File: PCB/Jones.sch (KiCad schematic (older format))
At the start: 250 parts, among them J1 USB_C_Receptacle_USB2.0, J2 Conn_01x03, J3 Conn_01x02, J5 Conn_02x03_Odd_Even, U1 ATmega32U4-MU, U2 24LC64, Y1 16MHz

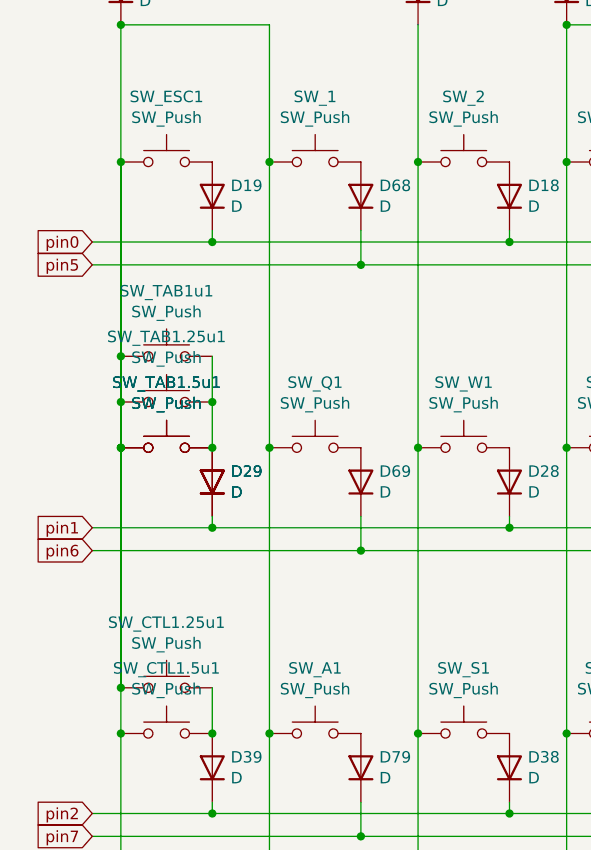
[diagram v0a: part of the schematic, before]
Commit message: issue レイアウト：40sキット対応 #29
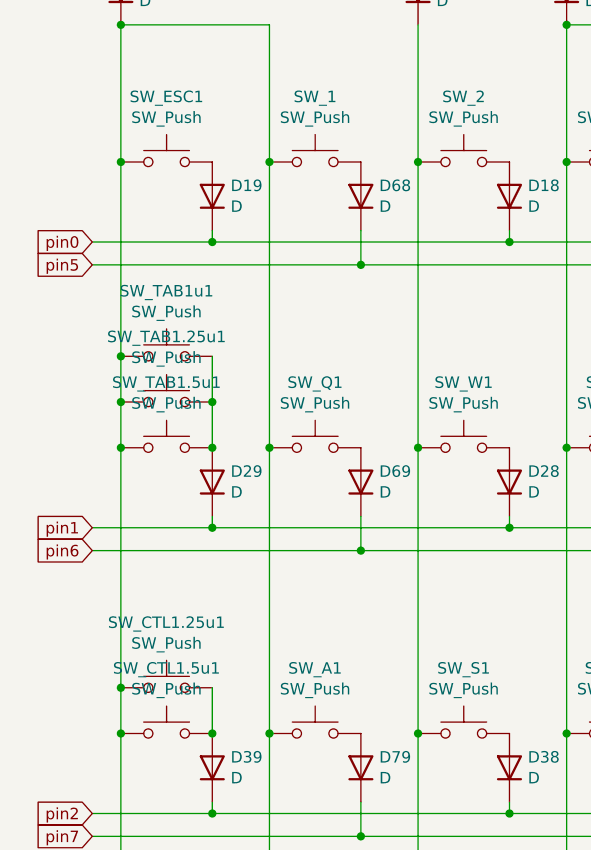
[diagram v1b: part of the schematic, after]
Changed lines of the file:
@@
 $EndComp
 $Comp
-L Device:D D29
-U 1 1 5F65B339
-P 1325 3475
-F 0 "D29" V 1371 3395 50  0000 R CNN
-F 1 "D" V 1280 3395 50  0000 R CNN
-F 2 "Diode_SMD:D_SOD-123" H 1325 3475 50  0001 C CNN
-F 3 "~" H 1325 3475 50  0001 C CNN
-F 4 "C81598" H 1325 3475 50  0001 C CNN "LCSC"
-	1    1325 3475
-	0    -1   -1   0
-$EndComp
-$Comp
 L Switch:SW_Push SW_Q1
 U 1 1 5F65B33F
@@
 	0    -1   -1   0
 $EndComp
-$Comp
-L Switch:SW_Push SW_TAB1.5u1
-U 1 1 5F65B333
-P 1125 3325
-F 0 "SW_TAB1.5u1" H 1125 3610 50  0000 C CNN
-F 1 "SW_Push" H 1125 3519 50  0000 C CNN
-F 2 "MX_Alps_Hybrid:MXOnly-1.5U-Hotswap-guide" H 1125 3525 50  0001 C CNN
-F 3 "~" H 1125 3525 50  0001 C CNN
-	1    1125 3325
-	1    0    0    -1
-$EndComp
 Wire Wire Line
 	925  1475 1575 1475
@@
 Wire Wire Line
 	800  2425 1325 2425
-Connection ~ 925  3325
 Wire Wire Line
 	800  3675 1325 3675
-Wire Wire Line
-	925  3325 925  4375
 Connection ~ 925  4375
 Connection ~ 925  4575
@@
 Text Notes 14450 3725 0    50   ~ 0
 Audio\nC4,5,6\nB5,6,7
-Wire Wire Line
-	925  2075 925  3325
 Connection ~ 925  2075
 $Comp

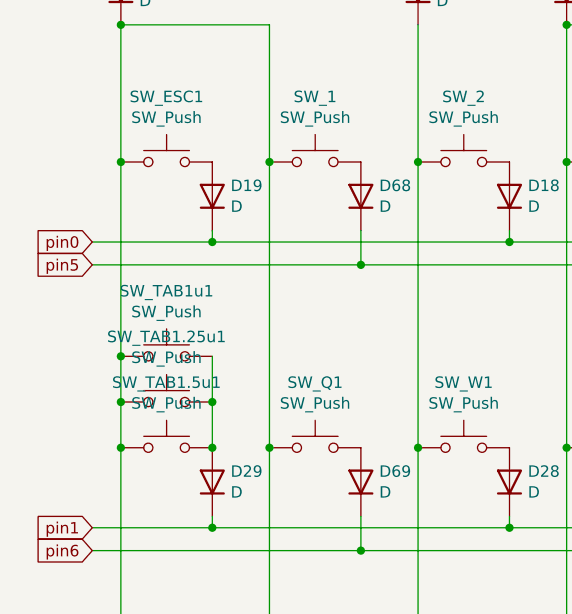
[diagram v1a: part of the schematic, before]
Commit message: Revert "Merge pull request #36 from jpskenn/dev_1.1_Add_40s_layout_#29"
This reverts commit ac7df7e95556fcbf06f35e39de5424a1bd39dfc1, reversing
changes made to 127994836709470240343b38cf9ba11c4b8eb1ff.
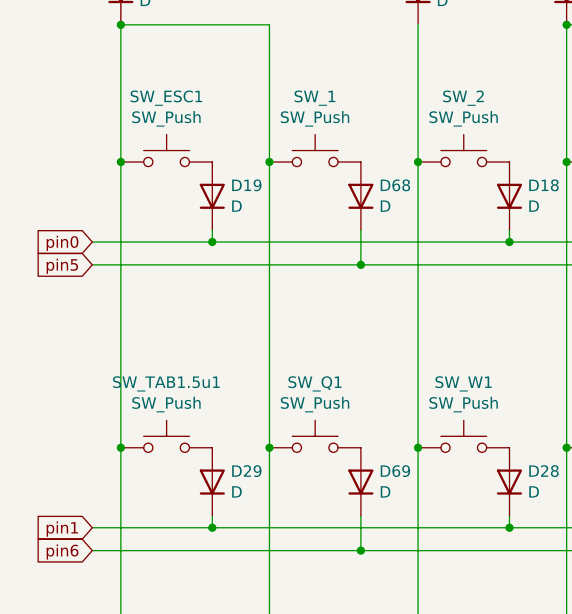
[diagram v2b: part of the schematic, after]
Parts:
- removed SW_TAB1.25u1: SW_Push, MX_Alps_Hybrid:MXOnly-1.25U-Hotswap-guide-Rotate, symbol Switch:SW_Push
- removed SW_TAB1u1: SW_Push, MX_Alps_Hybrid:MXOnly-1U-Hotswap-guide-4pin, symbol Switch:SW_Push
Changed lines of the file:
@@
 $EndComp
 $Comp
+L Device:D D29
+U 1 1 5F65B339
+P 1325 3475
+F 0 "D29" V 1371 3395 50  0000 R CNN
+F 1 "D" V 1280 3395 50  0000 R CNN
+F 2 "Diode_SMD:D_SOD-123" H 1325 3475 50  0001 C CNN
+F 3 "~" H 1325 3475 50  0001 C CNN
+F 4 "C81598" H 1325 3475 50  0001 C CNN "LCSC"
+	1    1325 3475
+	0    -1   -1   0
+$EndComp
+$Comp
 L Switch:SW_Push SW_Q1
 U 1 1 5F65B33F
@@
 	0    -1   -1   0
 $EndComp
+$Comp
+L Switch:SW_Push SW_TAB1.5u1
+U 1 1 5F65B333
+P 1125 3325
+F 0 "SW_TAB1.5u1" H 1125 3610 50  0000 C CNN
+F 1 "SW_Push" H 1125 3519 50  0000 C CNN
+F 2 "MX_Alps_Hybrid:MXOnly-1.5U-Hotswap-guide" H 1125 3525 50  0001 C CNN
+F 3 "~" H 1125 3525 50  0001 C CNN
+	1    1125 3325
+	1    0    0    -1
+$EndComp
 Wire Wire Line
 	925  1475 1575 1475
@@
 Wire Wire Line
 	800  2425 1325 2425
+Connection ~ 925  3325
 Wire Wire Line
 	800  3675 1325 3675
+Wire Wire Line
+	925  3325 925  4375
 Connection ~ 925  4375
 Connection ~ 925  4575
@@
 Text Notes 14450 3725 0    50   ~ 0
 Audio\nC4,5,6\nB5,6,7
+Wire Wire Line
+	925  2075 925  3325
 Connection ~ 925  2075
 $Comp
@@
 Wire Wire Line
 	14725 1575 14825 1575
-Wire Wire Line
-	925  2075 925  2925
-Wire Wire Line
-	925  3325 925  4375
-Connection ~ 925  3325
-$Comp
-L Switch:SW_Push SW_TAB1.5u1
-U 1 1 5F65B333
-P 1125 3325
-F 0 "SW_TAB1.5u1" H 1125 3610 50  0000 C CNN
-F 1 "SW_Push" H 1125 3519 50  0000 C CNN
-F 2 "MX_Alps_Hybrid:MXOnly-1.5U-Hotswap-guide" H 1125 3525 50  0001 C CNN
-F 3 "~" H 1125 3525 50  0001 C CNN
-	1    1125 3325
-	1    0    0    -1
-$EndComp
-$Comp
-L Device:D D29
-U 1 1 5F65B339
-P 1325 3475
-F 0 "D29" V 1371 3395 50  0000 R CNN
-F 1 "D" V 1280 3395 50  0000 R CNN
-F 2 "Diode_SMD:D_SOD-123" H 1325 3475 50  0001 C CNN
-F 3 "~" H 1325 3475 50  0001 C CNN
-F 4 "C81598" H 1325 3475 50  0001 C CNN "LCSC"
-	1    1325 3475
-	0    -1   -1   0
-$EndComp
-$Comp
-L Switch:SW_Push SW_TAB1.25u1
-U 1 1 615879B4
-P 1125 3125
-F 0 "SW_TAB1.25u1" H 1125 3410 50  0000 C CNN
-F 1 "SW_Push" H 1125 3319 50  0000 C CNN
-F 2 "MX_Alps_Hybrid:MXOnly-1.25U-Hotswap-guide-Rotate" H 1125 3325 50  0001 C CNN
-F 3 "~" H 1125 3325 50  0001 C CNN
-	1    1125 3125
-	1    0    0    -1
-$EndComp
-$Comp
-L Switch:SW_Push SW_TAB1u1
-U 1 1 615B818E
-P 1125 2925
-F 0 "SW_TAB1u1" H 1125 3210 50  0000 C CNN
-F 1 "SW_Push" H 1125 3119 50  0000 C CNN
-F 2 "MX_Alps_Hybrid:MXOnly-1U-Hotswap-guide-4pin" H 1125 3125 50  0001 C CNN
-F 3 "~" H 1125 3125 50  0001 C CNN
-	1    1125 2925
-	1    0    0    -1
-$EndComp
-Connection ~ 925  2925
-Wire Wire Line
-	925  2925 925  3125
-Connection ~ 925  3125
-Wire Wire Line
-	925  3125 925  3325
-Wire Wire Line
-	1325 2925 1325 3125
-Connection ~ 1325 3325
-Connection ~ 1325 3125
-Wire Wire Line
-	1325 3125 1325 3325
 $EndSCHEMATC

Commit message: 回路図更新。PCBテスト中
回路図、R2のTabに1uと1.25uを追加。
PCB、1uの配置が決まらず、試行錯誤中。
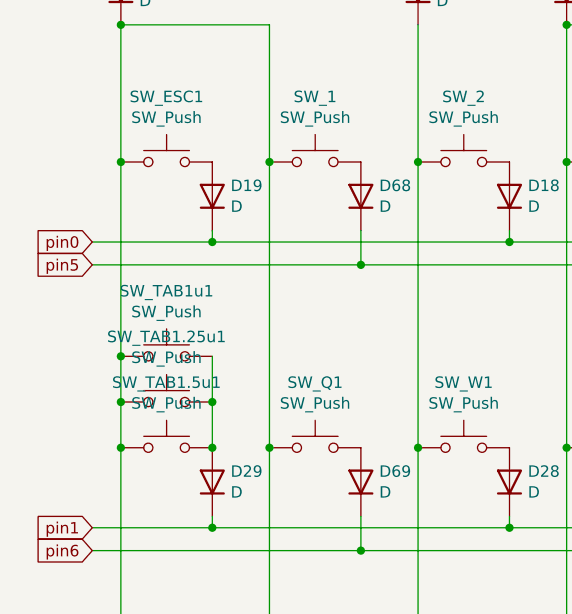
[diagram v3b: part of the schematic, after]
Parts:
- added SW_TAB1.25u1: SW_Push, MX_Alps_Hybrid:MXOnly-1.25U-Hotswap-guide-Rotate, symbol Switch:SW_Push
- added SW_TAB1u1: SW_Push, MX_Alps_Hybrid:MXOnly-1U-Hotswap-guide, symbol Switch:SW_Push
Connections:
- net RE2_1: now also SW_TAB1.25u1.1, SW_TAB1u1.1
- net at D29.2 (A), SW_TAB1.5u1.2: now also SW_TAB1.25u1.2, SW_TAB1u1.2
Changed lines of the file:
@@
 $EndComp
 $Comp
-L Device:D D29
-U 1 1 5F65B339
-P 1325 3475
-F 0 "D29" V 1371 3395 50  0000 R CNN
-F 1 "D" V 1280 3395 50  0000 R CNN
-F 2 "Diode_SMD:D_SOD-123" H 1325 3475 50  0001 C CNN
-F 3 "~" H 1325 3475 50  0001 C CNN
-F 4 "C81598" H 1325 3475 50  0001 C CNN "LCSC"
-	1    1325 3475
-	0    -1   -1   0
-$EndComp
-$Comp
 L Switch:SW_Push SW_Q1
 U 1 1 5F65B33F
@@
 	0    -1   -1   0
 $EndComp
-$Comp
-L Switch:SW_Push SW_TAB1.5u1
-U 1 1 5F65B333
-P 1125 3325
-F 0 "SW_TAB1.5u1" H 1125 3610 50  0000 C CNN
-F 1 "SW_Push" H 1125 3519 50  0000 C CNN
-F 2 "MX_Alps_Hybrid:MXOnly-1.5U-Hotswap-guide" H 1125 3525 50  0001 C CNN
-F 3 "~" H 1125 3525 50  0001 C CNN
-	1    1125 3325
-	1    0    0    -1
-$EndComp
 Wire Wire Line
 	925  1475 1575 1475
@@
 Wire Wire Line
 	800  2425 1325 2425
-Connection ~ 925  3325
 Wire Wire Line
 	800  3675 1325 3675
-Wire Wire Line
-	925  3325 925  4375
 Connection ~ 925  4375
 Connection ~ 925  4575
@@
 Text Notes 14450 3725 0    50   ~ 0
 Audio\nC4,5,6\nB5,6,7
-Wire Wire Line
-	925  2075 925  3325
 Connection ~ 925  2075
 $Comp
@@
 Wire Wire Line
 	14725 1575 14825 1575
+Wire Wire Line
+	925  2075 925  2925
+Wire Wire Line
+	925  3325 925  4375
+Connection ~ 925  3325
+$Comp
+L Switch:SW_Push SW_TAB1.5u1
+U 1 1 5F65B333
+P 1125 3325
+F 0 "SW_TAB1.5u1" H 1125 3610 50  0000 C CNN
+F 1 "SW_Push" H 1125 3519 50  0000 C CNN
+F 2 "MX_Alps_Hybrid:MXOnly-1.5U-Hotswap-guide" H 1125 3525 50  0001 C CNN
+F 3 "~" H 1125 3525 50  0001 C CNN
+	1    1125 3325
+	1    0    0    -1
+$EndComp
+$Comp
+L Device:D D29
+U 1 1 5F65B339
+P 1325 3475
+F 0 "D29" V 1371 3395 50  0000 R CNN
+F 1 "D" V 1280 3395 50  0000 R CNN
+F 2 "Diode_SMD:D_SOD-123" H 1325 3475 50  0001 C CNN
+F 3 "~" H 1325 3475 50  0001 C CNN
+F 4 "C81598" H 1325 3475 50  0001 C CNN "LCSC"
+	1    1325 3475
+	0    -1   -1   0
+$EndComp
+$Comp
+L Switch:SW_Push SW_TAB1.25u1
+U 1 1 615879B4
+P 1125 3125
+F 0 "SW_TAB1.25u1" H 1125 3410 50  0000 C CNN
+F 1 "SW_Push" H 1125 3319 50  0000 C CNN
+F 2 "MX_Alps_Hybrid:MXOnly-1.25U-Hotswap-guide-Rotate" H 1125 3325 50  0001 C CNN
+F 3 "~" H 1125 3325 50  0001 C CNN
+	1    1125 3125
+	1    0    0    -1
+$EndComp
+$Comp
+L Switch:SW_Push SW_TAB1u1
+U 1 1 615B818E
+P 1125 2925
+F 0 "SW_TAB1u1" H 1125 3210 50  0000 C CNN
+F 1 "SW_Push" H 1125 3119 50  0000 C CNN
+F 2 "MX_Alps_Hybrid:MXOnly-1U-Hotswap-guide" H 1125 3125 50  0001 C CNN
+F 3 "~" H 1125 3125 50  0001 C CNN
+	1    1125 2925
+	1    0    0    -1
+$EndComp
+Connection ~ 925  2925
+Wire Wire Line
+	925  2925 925  3125
+Connection ~ 925  3125
+Wire Wire Line
+	925  3125 925  3325
+Wire Wire Line
+	1325 2925 1325 3125
+Connection ~ 1325 3325
+Connection ~ 1325 3125
+Wire Wire Line
+	1325 3125 1325 3325
 $EndSCHEMATC

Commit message: 40s用、R2のTABに、1u、1.25uを追加
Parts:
- SW_TAB1u1: footprint MX_Alps_Hybrid:MXOnly-1U-Hotswap-guide -> MX_Alps_Hybrid:MXOnly-1U-Hotswap-guide-4pin
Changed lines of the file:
@@
 F 0 "SW_TAB1u1" H 1125 3210 50  0000 C CNN
 F 1 "SW_Push" H 1125 3119 50  0000 C CNN
-F 2 "MX_Alps_Hybrid:MXOnly-1U-Hotswap-guide" H 1125 3125 50  0001 C CNN
+F 2 "MX_Alps_Hybrid:MXOnly-1U-Hotswap-guide-4pin" H 1125 3125 50  0001 C CNN
 F 3 "~" H 1125 3125 50  0001 C CNN
 	1    1125 2925

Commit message: Dの方向マークを太くして視認性向上 #4
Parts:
- D0, D1, D11, D12, D13, D14, D15, D16, D17, D18, D19, D2, D21, D22, D23, D24, D25, D26, D27, D28, D29, D3, D30, D31, D32, D33, D34, D35, D36, D37, D38, D39, D4, D40, D41, D42, D43, D44, D45, D46, D47, D48, D49, D5, D50, D51, D52, D53, D56, D57, D59, D6, D61, D62, D63, D64, D65, D67, D68, D69, D7, D71, D73, D74, D75, D78, D79, D8, D83, D84, D85, D87, D89, D9, D91, D92, D93, D94, D95, D96, D97, D98: footprint Diode_SMD:D_SOD-123 -> locallib:D_SOD-123_bold_marking

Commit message: 三角マークを拡大 #5
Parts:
- LED1, LED2, LED3, LED4: footprint locallib:LED_SK6812MINI_PLCC4_3.5x3.5mm_P1.75mm_TriangleMark -> locallib:LED_SK6812MINI_PLCC4_3.5x3.5mm_P1.75mm_TriangleMark_Bold
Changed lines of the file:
@@
 F 0 "LED1" H 3594 8771 50  0000 L CNN
 F 1 "SK6812MINI" H 3594 8680 50  0000 L CNN
-F 2 "locallib:LED_SK6812MINI_PLCC4_3.5x3.5mm_P1.75mm_TriangleMark" H 3300 8425 50  0001 L TNN
+F 2 "locallib:LED_SK6812MINI_PLCC4_3.5x3.5mm_P1.75mm_TriangleMark_Bold" H 3300 8425 50  0001 L TNN
 F 3 "https://cdn-shop.adafruit.com/product-files/2686/SK6812MINI_REV.01-1-2.pdf" H 3350 8350 50  0001 L TNN
 	1    3250 8725
@@
 F 0 "LED2" H 4194 8771 50  0000 L CNN
 F 1 "SK6812MINI" H 4194 8680 50  0000 L CNN
-F 2 "locallib:LED_SK6812MINI_PLCC4_3.5x3.5mm_P1.75mm_TriangleMark" H 3900 8425 50  0001 L TNN
+F 2 "locallib:LED_SK6812MINI_PLCC4_3.5x3.5mm_P1.75mm_TriangleMark_Bold" H 3900 8425 50  0001 L TNN
 F 3 "https://cdn-shop.adafruit.com/product-files/2686/SK6812MINI_REV.01-1-2.pdf" H 3950 8350 50  0001 L TNN
 	1    3850 8725
@@
 F 0 "LED4" H 6019 9371 50  0000 L CNN
 F 1 "SK6812MINI" H 6019 9280 50  0000 L CNN
-F 2 "locallib:LED_SK6812MINI_PLCC4_3.5x3.5mm_P1.75mm_TriangleMark" H 5725 9025 50  0001 L TNN
+F 2 "locallib:LED_SK6812MINI_PLCC4_3.5x3.5mm_P1.75mm_TriangleMark_Bold" H 5725 9025 50  0001 L TNN
 F 3 "https://cdn-shop.adafruit.com/product-files/2686/SK6812MINI_REV.01-1-2.pdf" H 5775 8950 50  0001 L TNN
 	1    5675 9325
@@
 F 0 "LED3" H 5419 9371 50  0000 L CNN
 F 1 "SK6812MINI" H 5419 9280 50  0000 L CNN
-F 2 "locallib:LED_SK6812MINI_PLCC4_3.5x3.5mm_P1.75mm_TriangleMark" H 5125 9025 50  0001 L TNN
+F 2 "locallib:LED_SK6812MINI_PLCC4_3.5x3.5mm_P1.75mm_TriangleMark_Bold" H 5125 9025 50  0001 L TNN
 F 3 "https://cdn-shop.adafruit.com/product-files/2686/SK6812MINI_REV.01-1-2.pdf" H 5175 8950 50  0001 L TNN
 	1    5075 9325

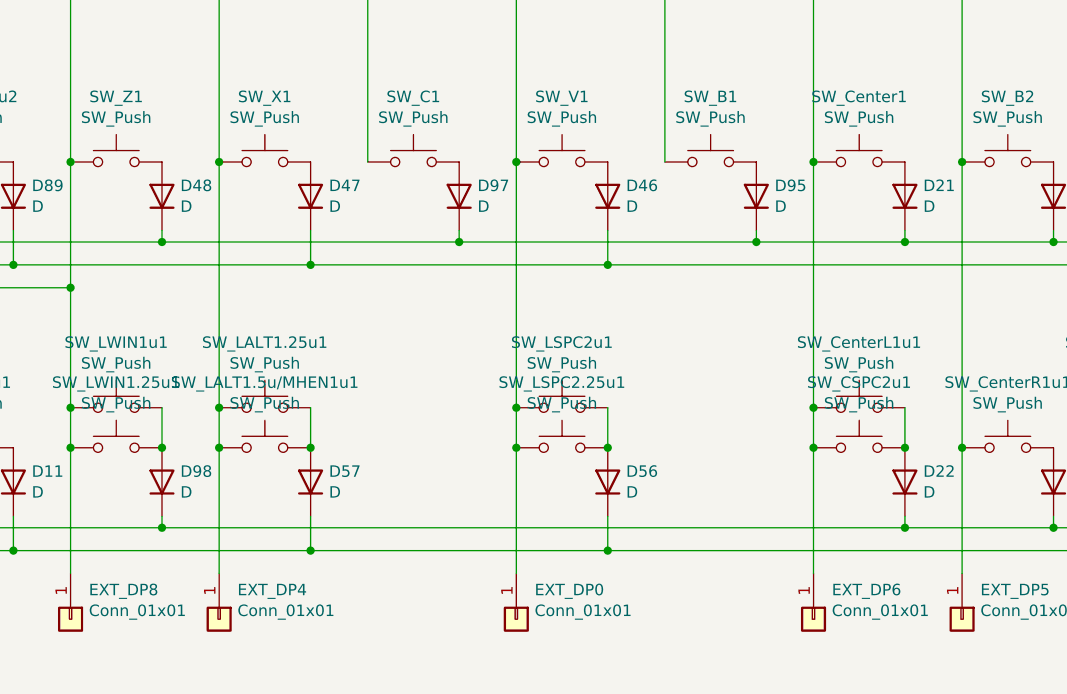
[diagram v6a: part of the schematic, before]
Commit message: WIP：左Modsの回路追加。PCB調整中
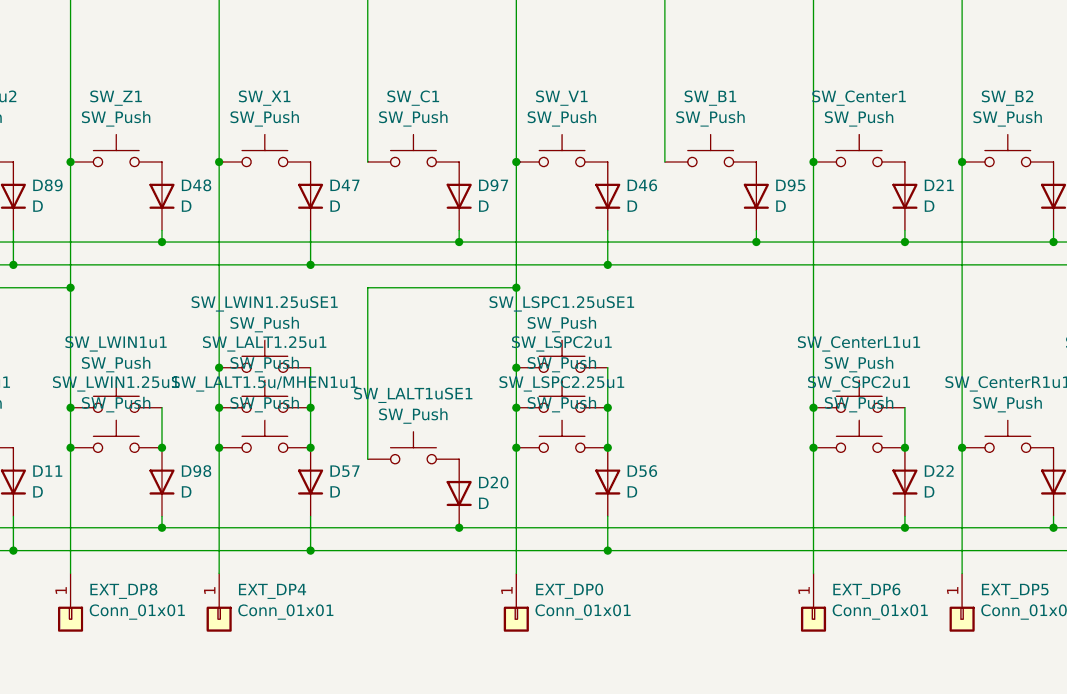
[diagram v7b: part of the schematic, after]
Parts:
- added D20: D, locallib:D_SOD-123_bold_marking, symbol Device:D
- added SW_LALT1uSE1: SW_Push, MX_Alps_Hybrid:MXOnly-1U-NoLED, symbol Switch:SW_Push
- added SW_LSPC1.25uSE1: SW_Push, MX_Alps_Hybrid:MXOnly-1.25U-Hotswap-guide, symbol Switch:SW_Push
- added SW_LWIN1.25uSE1: SW_Push, MX_Alps_Hybrid:MXOnly-1.25U-Hotswap-guide-Rotate, symbol Switch:SW_Push
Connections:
- net pin4: now also D20.1 (K)
- net at D7.1 (K), EXT_DP4.1 (Pin_1), SW_3.1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: now also SW_LWIN1.25uSE1.1
- net at D57.2 (A), SW_LALT1.25u1.2, SW_LALT1.5u/MHEN1u1.2: now also SW_LWIN1.25uSE1.2
- net at D6.1 (K), EXT_DP0.1 (Pin_1), SW_5.1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: now also SW_LALT1uSE1.1, SW_LSPC1.25uSE1.1
- net at D56.2 (A), SW_LSPC2.25u1.2, SW_LSPC2u1.2: now also SW_LSPC1.25uSE1.2
- new net: D20.2 (A), SW_LALT1uSE1.2
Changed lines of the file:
@@
 Connection ~ 3275 7075
 Wire Wire Line
-	2875 5825 2875 6900
+	2875 5825 2875 6725
 Wire Wire Line
 	6525 7425 7825 7425
@@
 $EndComp
 Wire Wire Line
-	4175 5825 4175 6900
+	4175 5825 4175 6375
 Connection ~ 6775 6900
 Wire Wire Line
@@
 	5875 6900 5875 7075
 Connection ~ 5875 7075
-Wire Wire Line
-	2625 7425 5875 7425
 $Comp
 L Connector_Generic:Conn_01x03 LED_STRIP1
@@
 Wire Wire Line
 	1325 3125 1325 3325
+$Comp
+L Switch:SW_Push SW_LWIN1.25uSE1
+U 1 1 6158BD01
+P 3075 6725
+F 0 "SW_LWIN1.25uSE1" H 3075 7010 50  0000 C CNN
+F 1 "SW_Push" H 3075 6919 50  0000 C CNN
+F 2 "MX_Alps_Hybrid:MXOnly-1.25U-Hotswap-guide-Rotate" H 3075 6925 50  0001 C CNN
+F 3 "~" H 3075 6925 50  0001 C CNN
+	1    3075 6725
+	1    0    0    -1
+$EndComp
+Wire Wire Line
+	3275 6900 3275 6725
+Connection ~ 2875 6725
+Wire Wire Line
+	2875 6725 2875 6900
+Connection ~ 3275 6900
+$Comp
+L Device:D D20
+U 1 1 615F2321
+P 3925 7275
+F 0 "D20" V 3971 7195 50  0000 R CNN
+F 1 "D" V 3880 7195 50  0000 R CNN
+F 2 "locallib:D_SOD-123_bold_marking" H 3925 7275 50  0001 C CNN
+F 3 "~" H 3925 7275 50  0001 C CNN
+F 4 "C81598" H 3925 7275 50  0001 C CNN "LCSC"
+	1    3925 7275
+	0    -1   -1   0
+$EndComp
+$Comp
+L Switch:SW_Push SW_LALT1uSE1
+U 1 1 615F2327
+P 3725 7125
+F 0 "SW_LALT1uSE1" H 3725 7410 50  0000 C CNN
+F 1 "SW_Push" H 3725 7319 50  0000 C CNN
+F 2 "MX_Alps_Hybrid:MXOnly-1U-NoLED" H 3725 7325 50  0001 C CNN
+F 3 "~" H 3725 7325 50  0001 C CNN
+	1    3725 7125
+	1    0    0    -1
+$EndComp
+Connection ~ 3925 7425
+Wire Wire Line
+	3925 7425 5875 7425
+Wire Wire Line
+	2625 7425 3925 7425
+Wire Wire Line
+	3525 7125 3525 6375
+Wire Wire Line
+	3525 6375 4175 6375
+Connection ~ 4175 6375
+Wire Wire Line
+	4175 6375 4175 6725
+$Comp
+L Switch:SW_Push SW_LSPC1.25uSE1
+U 1 1 617750B8
+P 4375 6725
+F 0 "SW_LSPC1.25uSE1" H 4375 7010 50  0000 C CNN
+F 1 "SW_Push" H 4375 6919 50  0000 C CNN
+F 2 "MX_Alps_Hybrid:MXOnly-1.25U-Hotswap-guide" H 4375 6925 50  0001 C CNN
+F 3 "~" H 4375 6925 50  0001 C CNN
+	1    4375 6725
+	1    0    0    -1
+$EndComp
+Wire Wire Line
+	4575 6725 4575 6900
+Connection ~ 4175 6725
+Wire Wire Line
+	4175 6725 4175 6900
+Connection ~ 4575 6900
 $EndSCHEMATC

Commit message: WIP：追加：テストピンを何らかの規格のピンヘッダに #18
テストピンまだ

左手側のみ変更
シルクまだ
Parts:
- removed EXT_P0, EXT_P1, EXT_P2, EXT_P3, EXT_P4, EXT_P5, EXT_P6, EXT_P7, EXT_P8, EXT_P9: Conn_01x01, TestPoint:TestPoint_THTPad_D1.5mm_Drill0.7mm, symbol Connector_Generic:Conn_01x01
- added J4, J6: Conn_01x05, Connector_PinHeader_2.54mm:PinHeader_1x05_P2.54mm_Vertical, symbol Connector_Generic:Conn_01x05
- SW_LSPC1.25uSE1: footprint MX_Alps_Hybrid:MXOnly-1.25U-Hotswap-guide -> MX_Alps_Hybrid:MXOnly-1.25U-NoLED
- SW_LWIN1.25uSE1: footprint MX_Alps_Hybrid:MXOnly-1.25U-Hotswap-guide-Rotate -> MX_Alps_Hybrid:MXOnly-1.25U-NoLED
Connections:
- net MISO: now also J4.1 (Pin_1)
- net MOSI: now also J4.2 (Pin_2)
- net SCK: now also J6.2 (Pin_2)
- net pin2: now also J4.3 (Pin_3)
- net pin3: now also J4.4 (Pin_4)
- net pin4: now also J4.5 (Pin_5)
- net pin5: now also J6.1 (Pin_1)
- net pin7: now also J6.3 (Pin_3)
- net pin8: now also J6.4 (Pin_4)
- net pin9: now also J6.5 (Pin_5)
